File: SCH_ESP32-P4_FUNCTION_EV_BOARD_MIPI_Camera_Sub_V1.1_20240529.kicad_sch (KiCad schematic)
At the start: 30 parts, among them J1 FPC_15P_R, J2 FPC_24P, Q3 DUAL_NMOS, SW1 NTC013-AT1J-A160T, U1 ME6211C18M5G-N, U2 ME6211C28M5G-N, Y1 24MHz

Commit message: sch: adapt the camera sub-board to the SC035HGS module
Rework the Espressif camera sub-board schematic for the SmartSens
SC035HGS global-shutter module (24-pin 0.5 mm FPC):

- J2: new symbol with the module pin names; pad n = module contact n
  (XUNPU FPC-05F-24PH20 drawing confirms FPC entry from footprint +y)
- U3 ME6211C15M5G-N adds DVDD 1.5 V; EN chain DOVDD -> DVDD -> AVDD
  (U3 EN from DOVDD via R12/C18, U2 EN from DVDD via R14/C15)
- U4-U6 SN74LVC1G07 open-drain buffers translate XSHUTDN, TRIG and
  LED_STROBE between the 3.3 V host and the 1.8 V sensor; this also
  removes the ~2.55 V that J1.5 put on XSHUTDN
- J3 JAE IL-G-4P-S3L2-SA control header (club IL-G footprint style)
- net renames RESET -> XSHUTDN/XSHUTDN_3V3, XVCLK -> MCLK, TRIG
- MPN/Manufacturer fields from the Espressif BOM; pattern-based
  netclasses; mod-only parts in libraries/SC035HGS_Mod.* with
  connector metadata in libraries/manifest.json

ERC 0; kicad-auto sch-review review-20261001-sc035hgs-mod-r2:
no failing findings, gate needs_user (module drawing applicability).

Co-Authored-By: Claude Opus 5.5 <noreply@anthropic.com>
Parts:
- added C16, C20: 10uF/6.3V(20%), Camera_Sub:C0603, symbol orcad_import:CAPACITOR
- added C17, C18, C19, C21, C22, C23: 0.1uF/50V(10%), Camera_Sub:C0402, symbol orcad_import:CAPACITOR
- added J3: IL-G-4P-S3L2-SA, SC035HGS_Mod:IL-G-4P, symbol SC035HGS_Mod:CONN_01X04
- added R12, R24, R28: 10K(1%), Camera_Sub:R0402, symbol orcad_import:RESISTOR
- added R25, R27: 100K(1%), Camera_Sub:R0402, symbol orcad_import:RESISTOR
- added R26: 2.2K(1%), Camera_Sub:R0402, symbol orcad_import:RESISTOR
- added U3: ME6211C15M5G-N, Camera_Sub:SOT23-5, symbol SC035HGS_Mod:ME6211C15M5G-N
- added U4, U5, U6: SN74LVC1G07DBVR, Camera_Sub:SOT23-5, symbol SC035HGS_Mod:SN74LVC1G07DBVR
- J1: MPN (none) -> AFA07-S15FCA-00; Manufacturer (none) -> JUSHUO (钜硕电子)
- J2: symbol orcad_import:FPC_24P -> SC035HGS_Mod:SC035HGS_FPC_24P; MPN (none) -> FPC-05F-24PH20; Manufacturer (none) -> XUNPU (讯普)
- Q3: MPN (none) -> DMN63D8LDW-7; Manufacturer (none) -> Diodes Incorporated
- SW1: MPN (none) -> YTS-A016-2; Manufacturer (none) -> YIYUAN (怡远)
- U1: MPN (none) -> ME6211C18M5G-N; Manufacturer (none) -> Microne (Nanjing Micro One)
- U2: MPN (none) -> ME6211C28M5G-N; Manufacturer (none) -> Microne (Nanjing Micro One)
- Y1: MPN (none) -> 2.1.3.2400037; Manufacturer (none) -> MDH
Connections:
- net 3V3: now also C16.1, C17.1, R24.2, R28.2, U3.1 (VIN)
- net AVDD_2V8: no longer J2.23
- net CSI_CLKN: now also J2.18 (MIPI_RCN); no longer J2.6
- net CSI_CLKP: now also J2.19 (MIPI_RCP); no longer J2.7
- net CSI_DATA1N: now also J2.11 (MIPI_RDN1); no longer J2.3
- net CSI_DATA1P: now also J2.12 (MIPI_RDP1); no longer J2.4
- net DOVDD_1V8: now also J2.22 (DOVDD_1V8), C21.1, C22.1, C23.1, R12.2, R26.2, U4.5 (VCC), U5.5 (VCC), U6.5 (VCC); no longer J2.16, R14.2
- net GND: now also J2.17 (GND), J2.20 (GND), J2.7 (GND), C16.2, C17.2, C18.2, C19.2, C20.2, C21.2, C22.2, C23.2, J3.4 (Pin_4), R25.1, R27.1, U3.2 (GND), U4.3 (GND), U5.3 (GND), U6.3 (GND); no longer J2.13, J2.15, J2.19, J2.22, J2.5
- net SENSOR_SCL: now also J2.6 (SCL); no longer J2.21
- net SENSOR_SDA: now also J2.5 (SDA); no longer J2.20
- net LED_STROBE: now reaches J2.1 (LED_STROBE)
- net LED_STROBE: now also R27.2, U6.2
- net TRIG: now reaches J2.2 (TRIG)
- net TRIG: now also R26.1, U5.4
- net RESET renamed XSHUTDN
- net XSHUTDN: now also J2.3 (XSHUTDN), U4.4; no longer J1.5, J2.17
- net XVCLK renamed MCLK
- net MCLK: now also J2.21 (MCLK); no longer J2.14
- new net: C18.1, R12.1, U3.3 (EN)
- new net DVDD_1V5: C19.1, C20.1, J2.23 (DVDD_1V5), R14.2, U3.5 (OUT)
- new net LED_STROBE_3V3: J3.2 (Pin_2), R28.1, U6.4
- new net TRIG_3V3: J3.1 (Pin_1), R25.2, U5.2
- new net XSHUTDN_3V3: J1.5, J3.3 (Pin_3), R24.1, U4.2
- no-connect marks 10 -> 14
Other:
- note added: "DVDD LDO:"
- note added: "GS CTRL:"
- note added: "PWDN:"
- note removed: "RST:"
- title: ESP32-P4_FUNCTION_EV_BOARD_MIPI_Sub -> ESP32-P4_FUNCTION_EV_BOARD_MIPI_Sub - SC035HGS mod

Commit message: sch: switch J3 to the JAE IL-G S3L2 standard
Replace the club-style IL-G-4P footprint with
JAE_IL-G-4P-S3L2-SA_1x04_P2.50mm_Horizontal drawn from JAE drawing
SJ019575 ver.5: JAE terminal numbering (pin 1 at -X with the mating
face toward +Y; the club footprint had it mirrored), 1.1 mm holes,
club oval pads kept. The manifest records the +Y mating face from the
drawing, and the drawing is added under sources/. Netlist unchanged
apart from J3's footprint; ERC 0.

Co-Authored-By: Claude Opus 5.5 <noreply@anthropic.com>
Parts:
- J3: footprint SC035HGS_Mod:IL-G-4P -> SC035HGS_Mod:JAE_IL-G-4P-S3L2-SA_1x04_P2.50mm_Horizontal
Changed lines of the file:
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@@
 			)
 		)
-		(property "Footprint" "SC035HGS_Mod:IL-G-4P"
+		(property "Footprint" "SC035HGS_Mod:JAE_IL-G-4P-S3L2-SA_1x04_P2.50mm_Horizontal"
 			(at 203.2 142.24 0)
 			(hide yes)
@@
 			)
 		)
-		(property "Description" "GS control header, JAE IL-G 2.5 mm right-angle, friction lock (club IL-G footprint convention), to the ESP32-P4 GPIO header (3.3 V): 1 TRIG_3V3, 2 LED_STROBE_3V3, 3 XSHUTDN_3V3, 4 GND. Mating socket IL-G-4S-S3C2-SA"
+		(property "Description" "GS control header, JAE IL-G 2.5 mm right-angle, friction lock (JAE SJ019575 pin numbering), to the ESP32-P4 GPIO header (3.3 V): 1 TRIG_3V3, 2 LED_STROBE_3V3, 3 XSHUTDN_3V3, 4 GND. Mating socket IL-G-4S-S3C2-SA"
 			(at 203.2 142.24 0)
 			(hide yes)

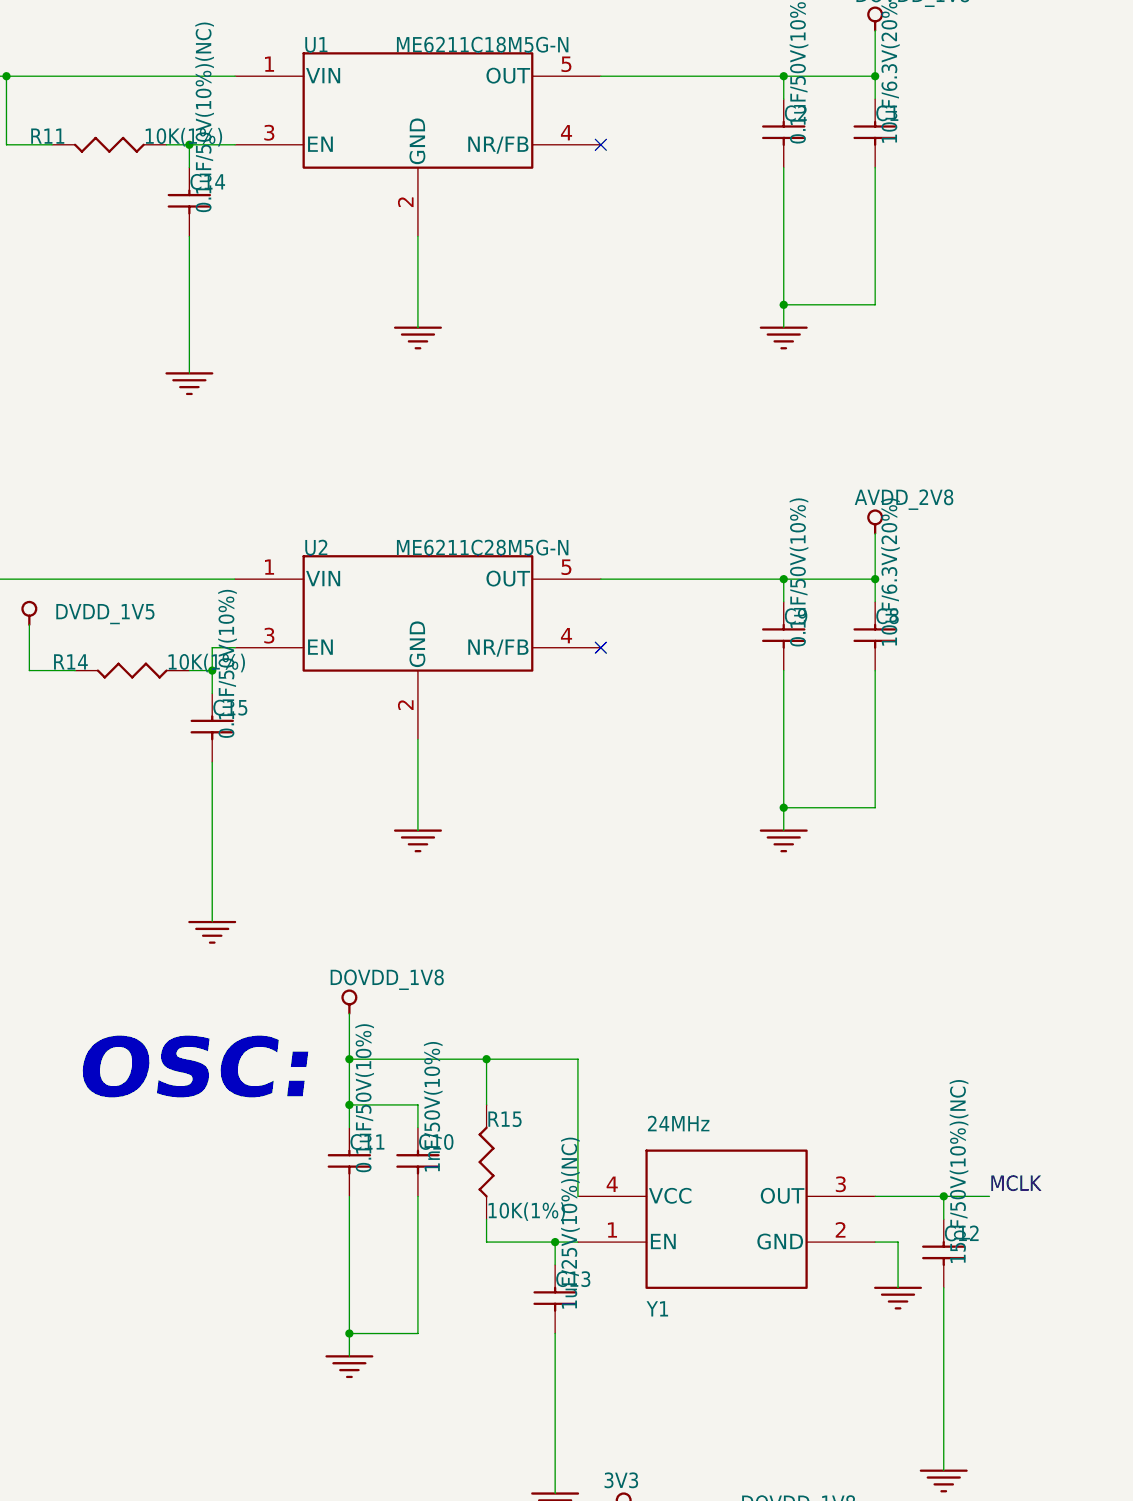
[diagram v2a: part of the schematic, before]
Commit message: pcb: lay out the SC035HGS adapter board
Update the PCB from the SC035HGS schematic and redo it: all of
Espressif's copper was removed and the parts re-placed and re-routed.
- 40 x 24 mm with R3 corners, 4 layers on JLC04161H-7628, 1.6 mm, ENIG
  (Board Setup minimums from pcb-fabrication-profile.json)
- J1 on the bottom edge, J2 on the top edge, J3 on the right edge
  opening outward (pin row 7.9 mm from the edge, per JAE SJ019575)
- In1 solid GND, In2 solid DOVDD_1V8; 3V3/DVDD_1V5/AVDD_2V8 as tracks
  in PWR_* netclasses
- MIPI CSI-2 pairs on the top layer, 100 ohm (0.2258/0.2032 mm), no
  vias, zero intra-pair skew; all vias 0.6/0.3 mm
- silkscreen text at 1.0/0.15 mm; MECH1/MECH2 dimension holders, the
  Allegro drill chart and off-board empty rule areas removed
- C12/C13/C14 (valued NC) set to DNP in schematic and PCB

DRC: 0 errors, 0 unconnected, 0 schematic parity issues; 86 silkscreen
warnings from Camera_Sub footprints whose silk extends past their
courtyards.

Co-Authored-By: Claude Opus 5.5 <noreply@anthropic.com>
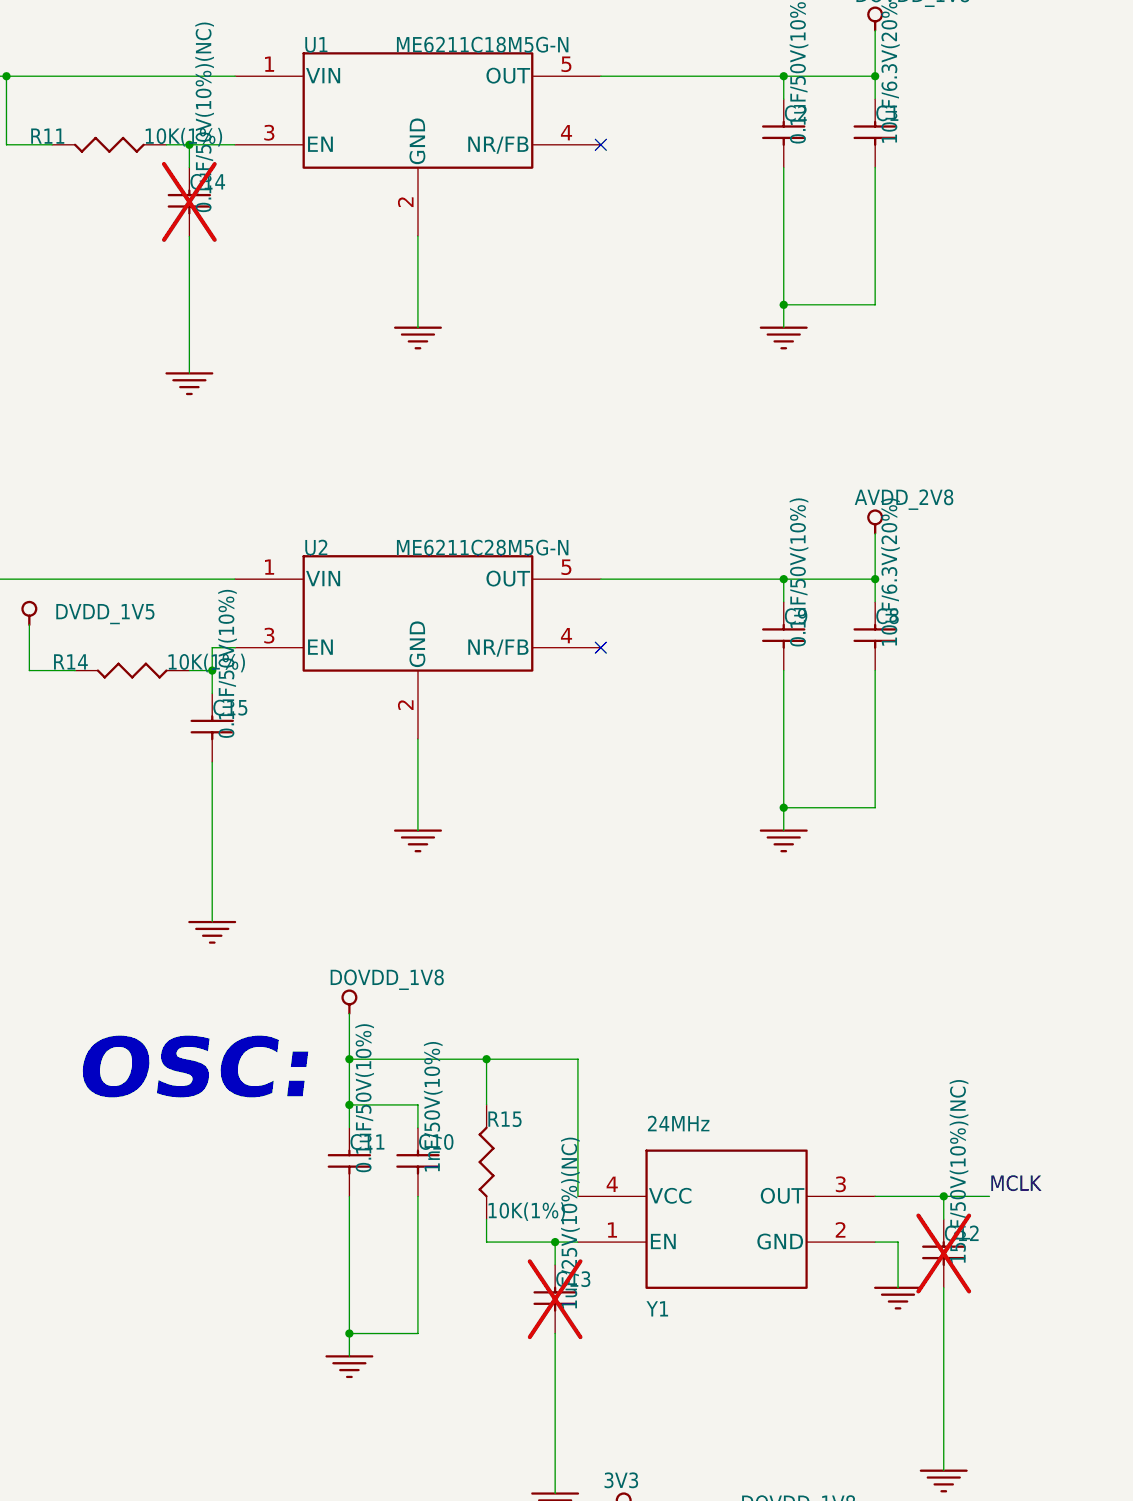
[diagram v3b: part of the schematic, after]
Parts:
- C12, C13, C14: now not fitted
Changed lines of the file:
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@@
 		(on_board yes)
 		(in_pos_files yes)
-		(dnp no)
+		(dnp yes)
 		(property "Reference" "C13"
 			(at 307.34 147.9676 0)
@@
 		(on_board yes)
 		(in_pos_files yes)
-		(dnp no)
+		(dnp yes)
 		(property "Reference" "C14"
 			(at 266.7 26.0476 0)
@@
 		(on_board yes)
 		(in_pos_files yes)
-		(dnp no)
+		(dnp yes)
 		(property "Reference" "C12"
 			(at 350.52 142.8876 0)
